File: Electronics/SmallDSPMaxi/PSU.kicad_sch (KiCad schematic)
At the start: 24 parts, among them J12 B4P-VH, U4 LM317_TO-252, U5 LM317_TO-252

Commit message: Adds final state of Maxi rev 1.0 and unbalanced IO boards rev 1.0.
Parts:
- removed C? (x3): 1u, Capacitor_SMD:C_0805_2012Metric, symbol Device:C_Small
- removed D? (x2): LED, LED_SMD:LED_0603_1608Metric, symbol Device:LED
- removed R39, R41: 1k2, Resistor_SMD:R_0402_1005Metric, symbol Device:R_Small
- removed R40, R42: 2k, Resistor_SMD:R_0603_1608Metric, symbol Device:R_Small
- removed R43, R44: 82R, Resistor_SMD:R_0603_1608Metric, symbol Device:R_Small
- removed U4, U5: LM317_TO-252, 1_Project_Footprints:TO-252-2 thermal vias, symbol Regulator_Linear:LM317_TO-252
- added C? (x2): 100n, Capacitor_SMD:C_0402_1005Metric, symbol Device:C_Small
- added C? (x3): 22u, Capacitor_SMD:C_0805_2012Metric, symbol Device:C_Small
- added R? (x2): 1R, Resistor_SMD:R_0402_1005Metric, symbol Device:R_Small
- added U7: LD1085D2T33TR, Package_TO_SOT_SMD:TO-263-2, symbol Regulator_Linear:LD1086D2T33TR
- added U8: TLV1117-33, Package_TO_SOT_SMD:SOT-223-3_TabPin2, symbol Regulator_Linear:TLV1117-33
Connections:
- net +3.3VA: now also C?.1, U8.2 (VO)
- net +3V3: now also C?.1
- net +5V: now also C?.1, U8.3 (VI)
- net GND: now also C?.2, C?.2, C?.2, C?.2, C?.2, U7.1 (ADJ/GND), U8.1 (GND)
- net at C?.1, FB?.2: now also C?.1, U7.3 (IN)
- net at FB?.1: now also R?.1, R?.1, U7.2 (OUT)
- new net: C?.1, R?.2, R?.2
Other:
- note removed: "Vout=1.25(1+R2/R1)+50uA*R2"
- moved on the sheet: C?

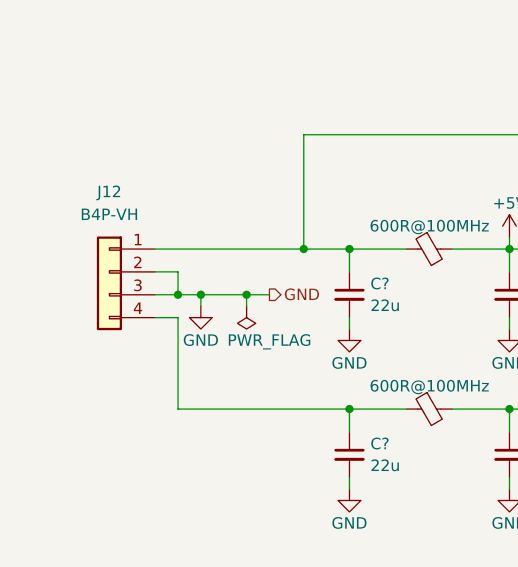
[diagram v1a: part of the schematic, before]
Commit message: Maxi: Replaces STM32 programming pin header with WE RedFit connectorand fixes minor issues. Adds driver for AKM AK4619 Codec and STM32CubeIDE workspace for Maxi firmware.
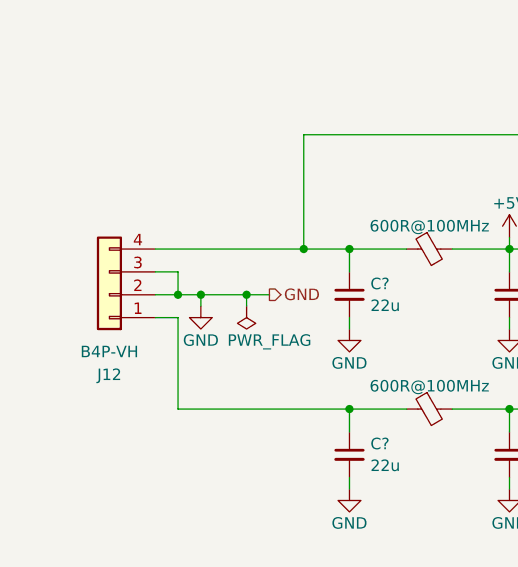
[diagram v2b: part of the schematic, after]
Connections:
- net at C?.1, FB?.1: now also J12.1 (Pin_1); no longer J12.4 (Pin_4)
- net at C?.1, C?.1, FB?.1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: now also J12.4 (Pin_4); no longer J12.1 (Pin_1)
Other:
- moved on the sheet: J12
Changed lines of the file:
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@@
   (title_block
     (title "SmallDSP Maxi")
-    (date "2024-01-06")
-    (rev "1.0")
+    (date "2024-02-19")
+    (rev "1.1")
     (company "Till Heuer")
   )
@@
     )
   )
-  (symbol (lib_id "Connector_Generic:Conn_01x04") (at 78.74 99.06 0) (mirror y) (unit 1)
-    (in_bom yes) (on_board yes) (dnp no) (fields_autoplaced)
-    (property "Reference" "J12" (at 78.74 90.17 0)
-      (effects (font (size 1.27 1.27)))
-    )
-    (property "Value" "B4P-VH" (at 78.74 92.71 0)
-      (effects (font (size 1.27 1.27)))
-    )
-    (property "Footprint" "Connector_JST:JST_VH_B4P-VH_1x04_P3.96mm_Vertical" (at 78.74 99.06 0)
-      (effects (font (size 1.27 1.27)) hide)
-    )
-    (property "Datasheet" "~" (at 78.74 99.06 0)
-      (effects (font (size 1.27 1.27)) hide)
-    )
-    (property "LCSC Part #" "-" (at 78.74 99.06 0)
-      (effects (font (size 1.27 1.27)) hide)
-    )
-    (property "Assembling" "" (at 78.74 99.06 0)
-      (effects (font (size 1.27 1.27)) hide)
-    )
-    (property "Manufacturer" "JST" (at 78.74 99.06 0)
-      (effects (font (size 1.27 1.27)) hide)
-    )
-    (property "Part Number" "B4P-VH" (at 78.74 99.06 0)
-      (effects (font (size 1.27 1.27)) hide)
-    )
+  (symbol (lib_id "Connector_Generic:Conn_01x04") (at 78.74 101.6 180) (unit 1)
+    (in_bom yes) (on_board yes) (dnp no)
+    (property "Reference" "J12" (at 78.74 110.49 0)
+      (effects (font (size 1.27 1.27)))
+    )
+    (property "Value" "B4P-VH" (at 78.74 107.95 0)
+      (effects (font (size 1.27 1.27)))
+    )
+    (property "Footprint" "Connector_JST:JST_VH_B4P-VH_1x04_P3.96mm_Vertical" (at 78.74 101.6 0)
+      (effects (font (size 1.27 1.27)) hide)
+    )
+    (property "Datasheet" "~" (at 78.74 101.6 0)
+      (effects (font (size 1.27 1.27)) hide)
+    )
+    (property "LCSC Part #" "-" (at 78.74 101.6 0)
+      (effects (font (size 1.27 1.27)) hide)
+    )
+    (property "Assembling" "" (at 78.74 101.6 0)
+      (effects (font (size 1.27 1.27)) hide)
+    )
+    (property "Manufacturer" "JST" (at 78.74 101.6 0)
+      (effects (font (size 1.27 1.27)) hide)
+    )
+    (property "Part Number" "B4P-VH" (at 78.74 101.6 0)
+      (effects (font (size 1.27 1.27)) hide)
+    )

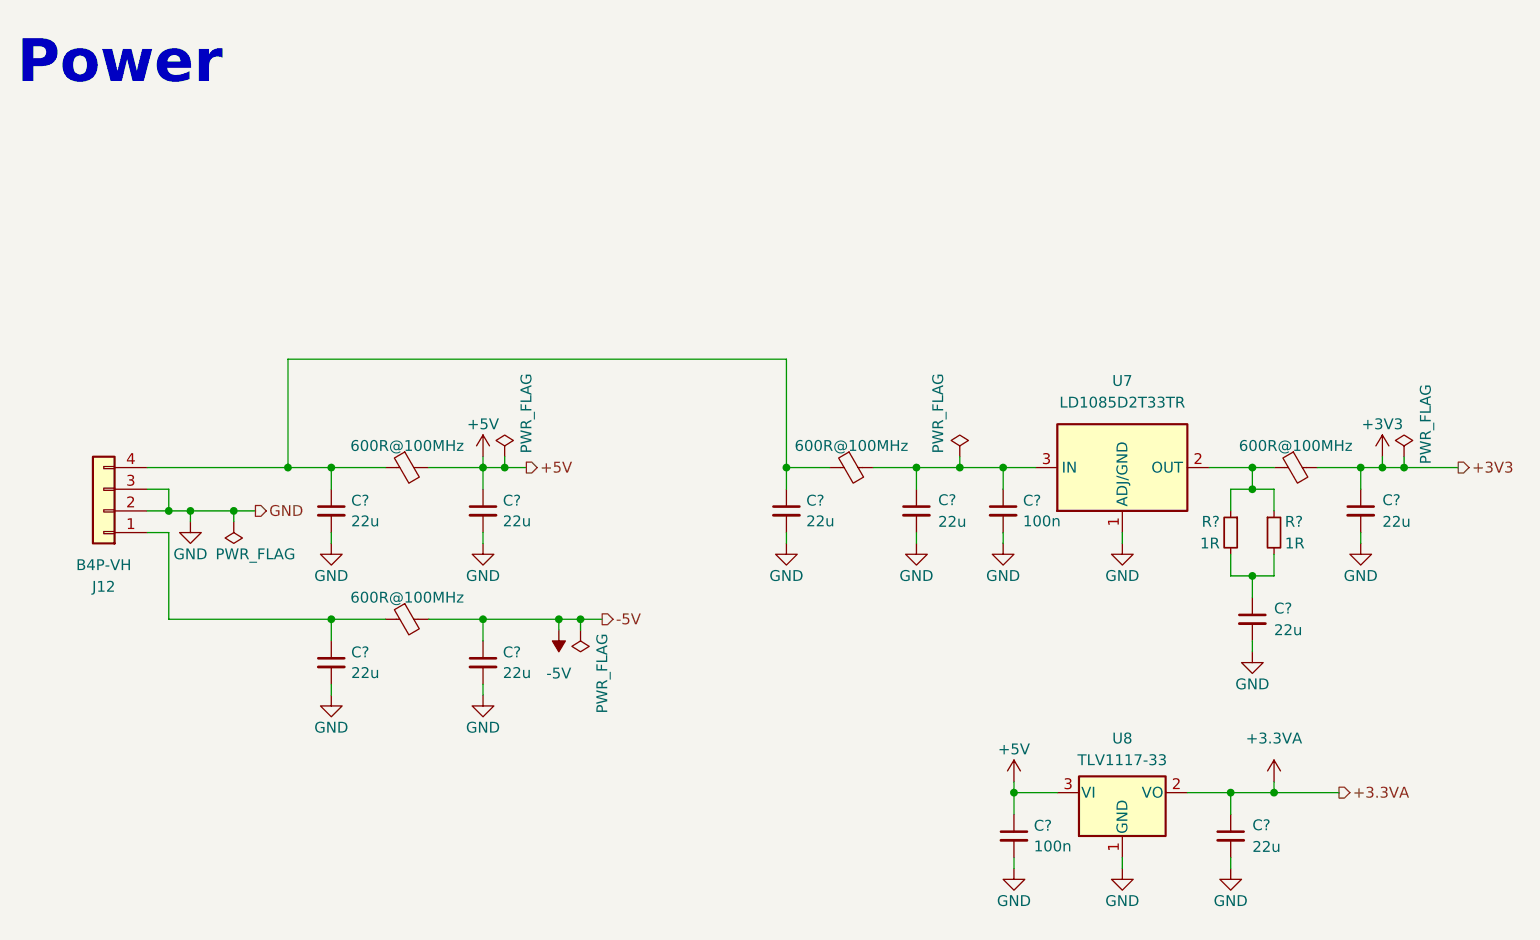
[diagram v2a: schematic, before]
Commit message: Adds AES17 measurements for rev1 of maxi. adds first iteration of maxi firmware. prototype now functional. adds mechanical information such as pcb 3d models and datasheets for psu and power switch, -connector.
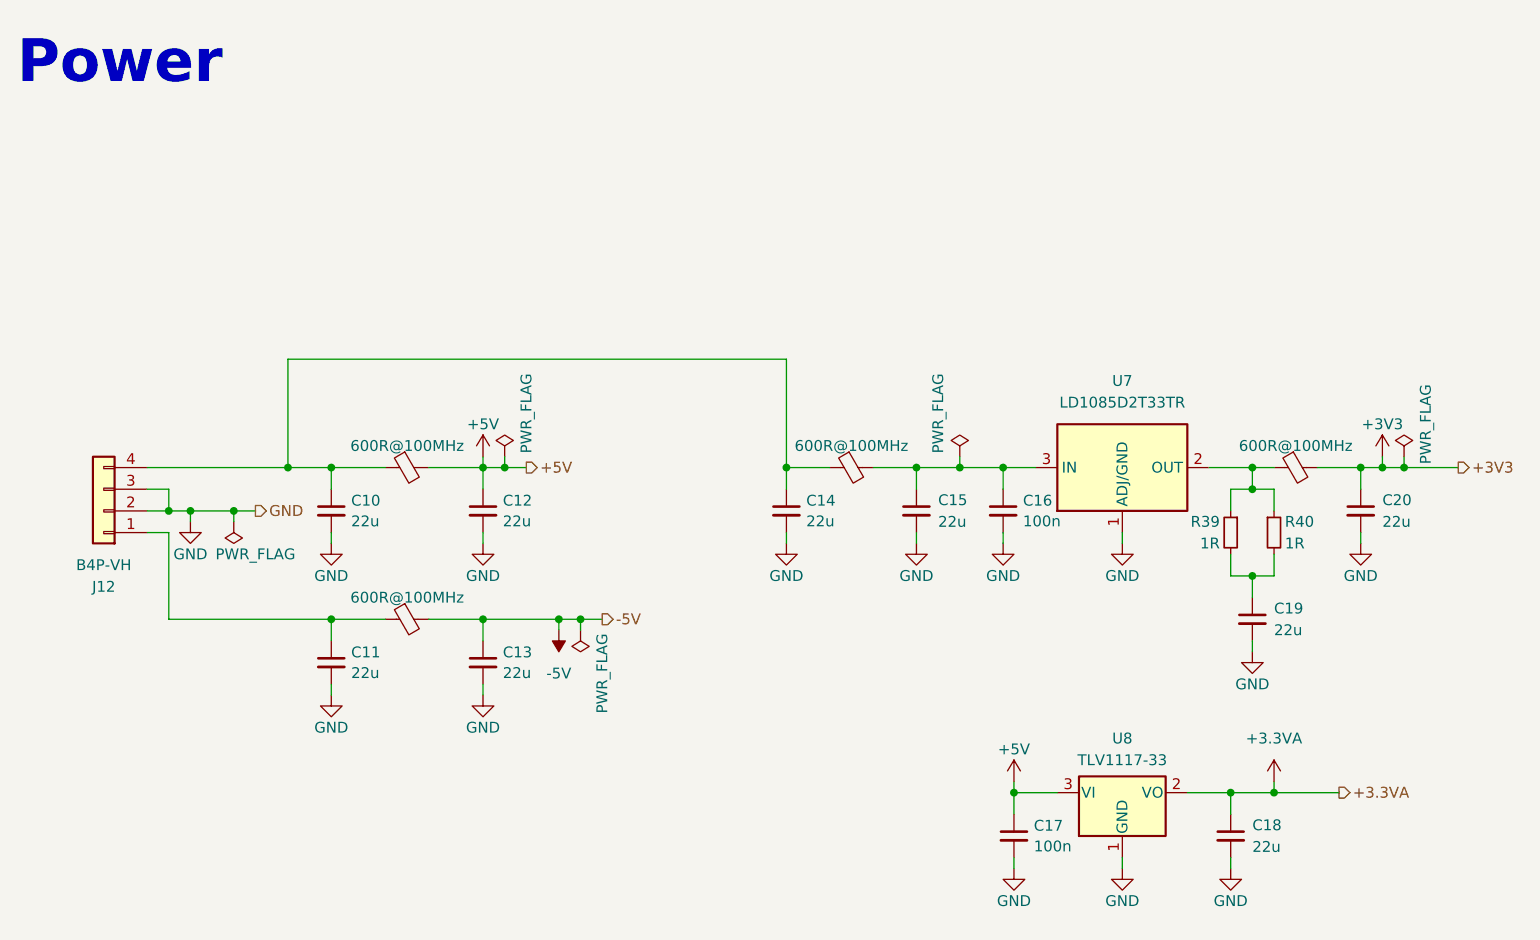
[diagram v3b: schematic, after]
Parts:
- gave numbers to parts that had none: 17
